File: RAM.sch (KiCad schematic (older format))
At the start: 2 parts

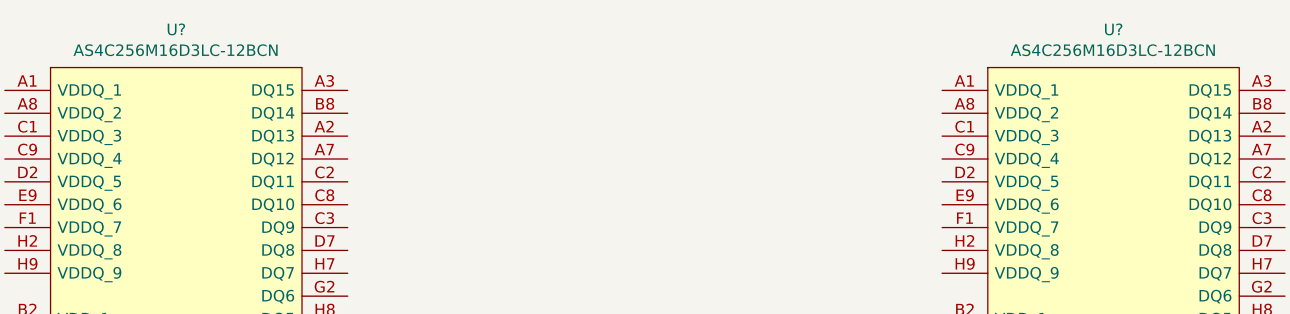
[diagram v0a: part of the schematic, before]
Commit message: Completeed the FPGA_Power sheet Created PCB
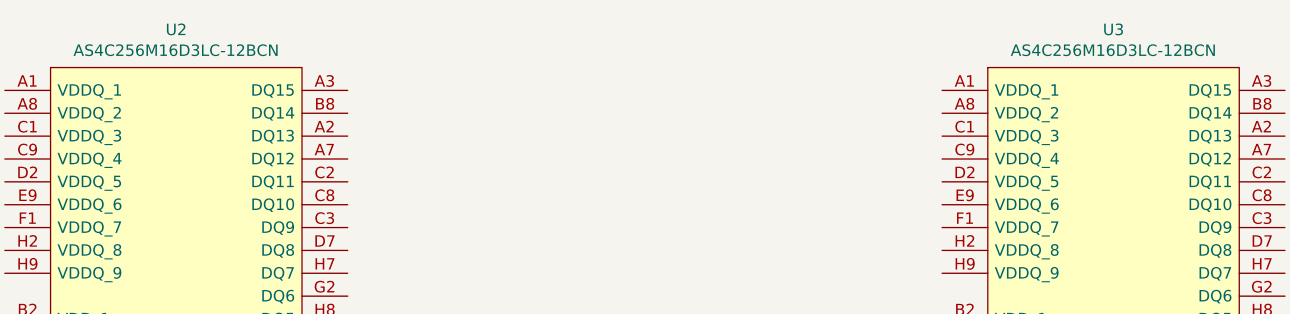
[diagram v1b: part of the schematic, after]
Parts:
- gave numbers to parts that had none: 2
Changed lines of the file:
@@
 $EndDescr
 $Comp
-L GM_Memory_RAM:AS4C256M16D3LC-12BCN U?
+L GM_Memory_RAM:AS4C256M16D3LC-12BCN U2
 U 1 1 601BEFCE
 P 3100 800
-F 0 "U?" H 3650 965 50  0000 C CNN
+F 0 "U2" H 3650 965 50  0000 C CNN
 F 1 "AS4C256M16D3LC-12BCN" H 3650 874 50  0000 C CNN
 F 2 "BGA96C80P9X16_750X1350X120" H 5250 1000 50  0001 L CNN
@@
 $EndComp
 $Comp
-L GM_Memory_RAM:AS4C256M16D3LC-12BCN U?
+L GM_Memory_RAM:AS4C256M16D3LC-12BCN U3
 U 1 1 601E10B7
 P 7200 800
-F 0 "U?" H 7750 965 50  0000 C CNN
+F 0 "U3" H 7750 965 50  0000 C CNN
 F 1 "AS4C256M16D3LC-12BCN" H 7750 874 50  0000 C CNN
 F 2 "BGA96C80P9X16_750X1350X120" H 9350 1000 50  0001 L CNN
